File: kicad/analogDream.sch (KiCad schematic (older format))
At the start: 37 parts, among them P2 CONN_4X2, P4 CONN_7X2, P6 CONN_4X2, U1 AD8422, U2 TL074

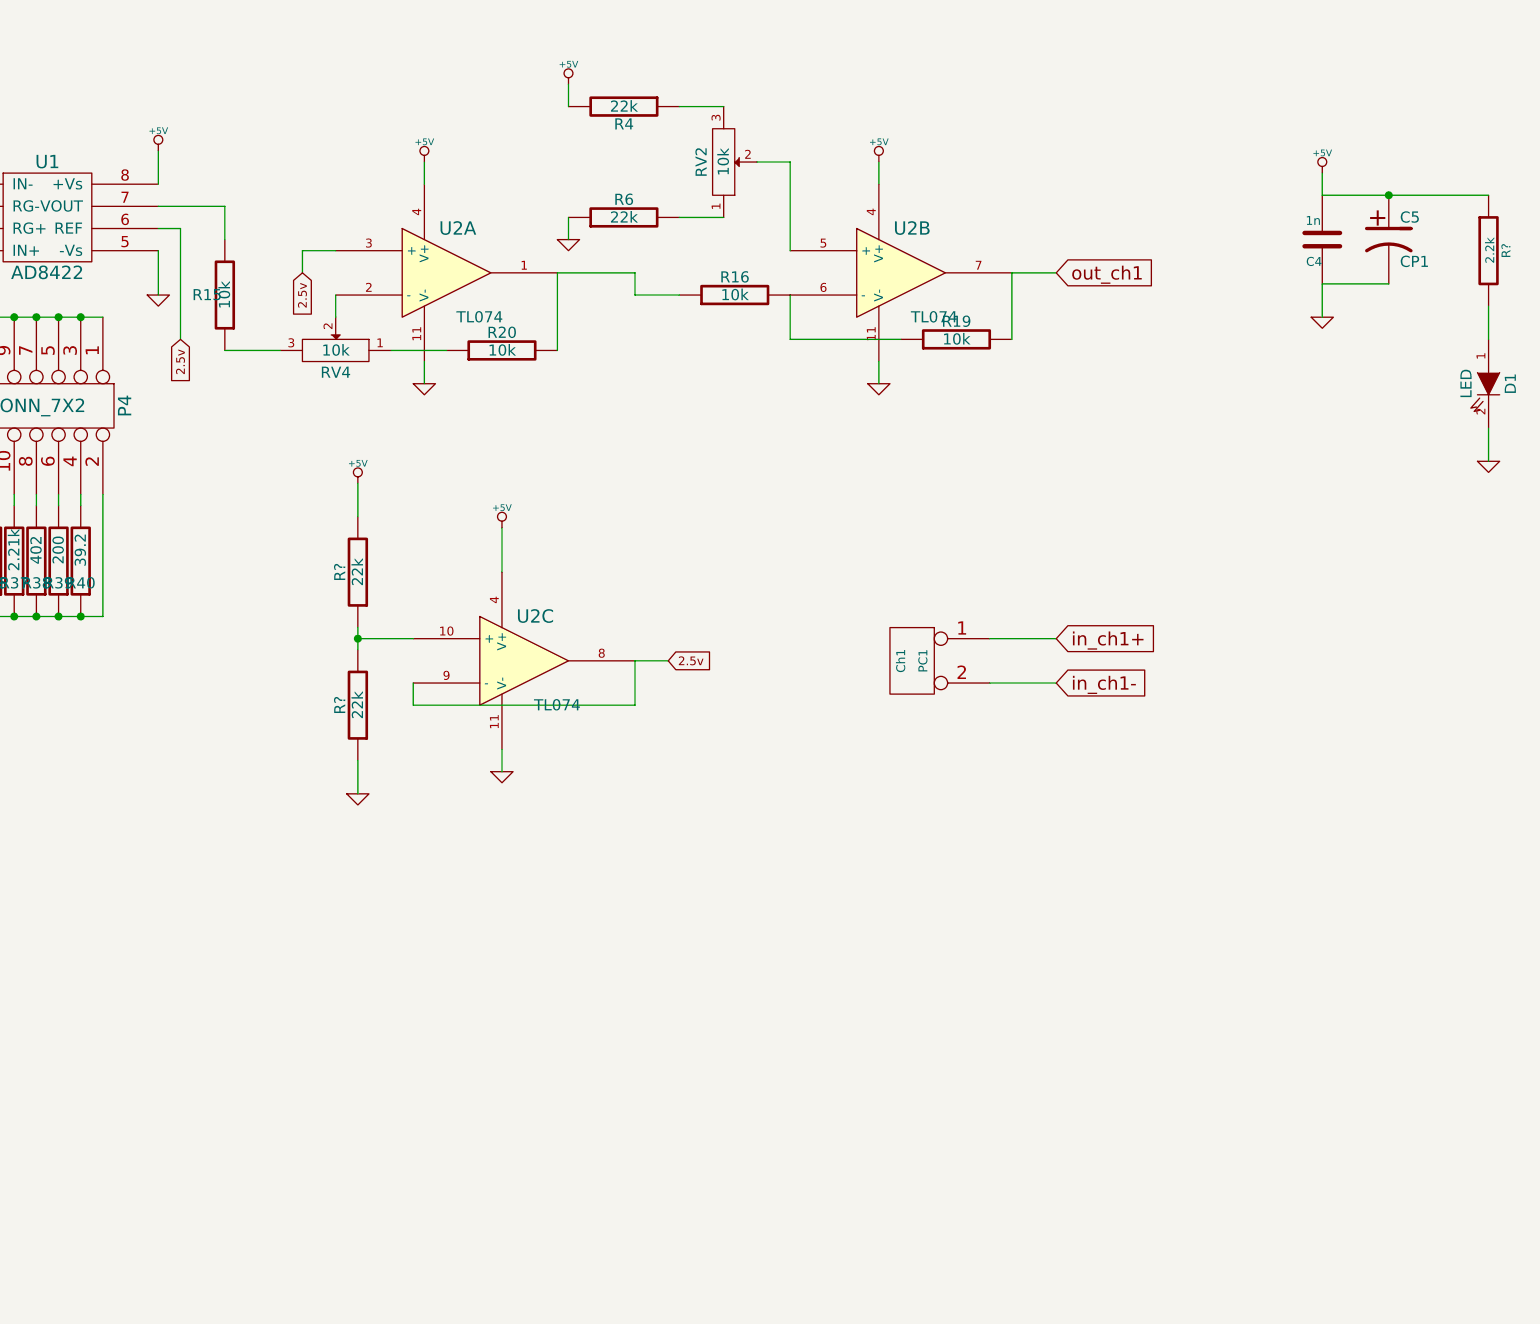
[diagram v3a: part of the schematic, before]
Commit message: Changed how offset voltage works
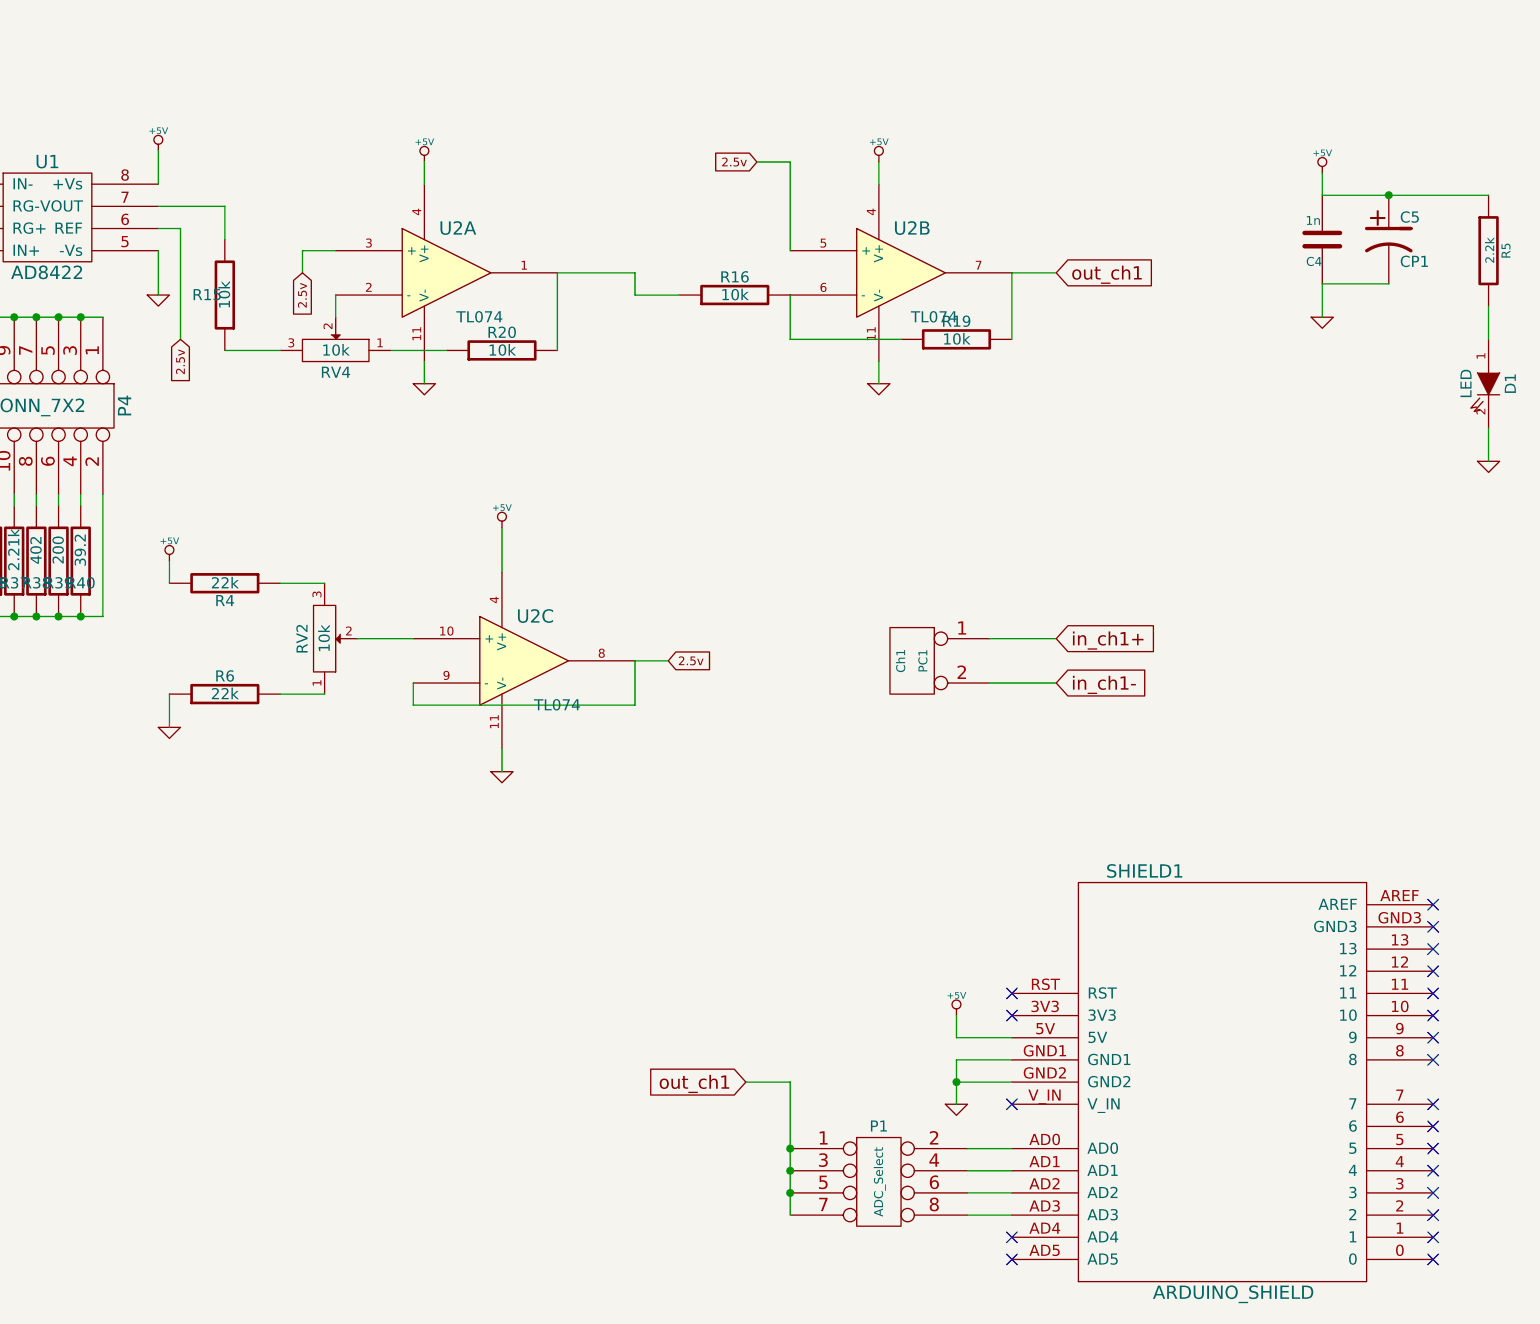
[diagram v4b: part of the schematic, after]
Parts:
- removed R? (x2): 22k, symbol R
- added P1: ADC_Select, symbol CONN_4X2
- added SHIELD1: ARDUINO_SHIELD, ~, symbol ARDUINO_SHIELD
- gave numbers to parts that had none: 1
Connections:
- net +5V: now also SHIELD1.5V
- net 2.5v: now also U2.5 (+)
- net GND: now also SHIELD1.GND1, SHIELD1.GND2
- net out_ch1: now also P1.1, P1.3, P1.5, P1.7
- net at RV2.2: now also U2.10 (+); no longer U2.5 (+)
- new net: P1.2, SHIELD1.AD0
- new net: P1.4, SHIELD1.AD1
- new net: P1.6, SHIELD1.AD2
- new net: P1.8, SHIELD1.AD3
- no-connect marks 0 -> 21
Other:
- moved on the sheet: R4, R6, RV2
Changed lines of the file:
@@
 	3450 1350 3450 1200
 Wire Wire Line
-	6000 1000 5800 1000
-Wire Wire Line
-	5800 1500 6000 1500
+	4200 3150 4000 3150
+Wire Wire Line
+	4000 3650 4200 3650
 Wire Wire Line
 	7300 2050 7300 1750
@@
 Wire Wire Line
 	6300 2050 6300 1850
-Wire Wire Line
-	5300 1500 5300 1600
 Wire Wire Line
 	6150 1250 6300 1250
@@
 L R R4
 U 1 1 4ECF00A1
-P 5550 1000
-F 0 "R4" V 5630 1000 50  0000 C CNN
-F 1 "22k" V 5550 1000 50  0000 C CNN
-F 2 "" H 5550 1000 60  0001 C CNN
-F 3 "" H 5550 1000 60  0001 C CNN
-	1    5550 1000
+P 3750 3150
+F 0 "R4" V 3830 3150 50  0000 C CNN
+F 1 "22k" V 3750 3150 50  0000 C CNN
+F 2 "" H 3750 3150 60  0001 C CNN
+F 3 "" H 3750 3150 60  0001 C CNN
+	1    3750 3150
 	0    1    1    0
 $EndComp
 $Comp
-L GND #PWR026
+L GND #PWR01
 U 1 1 4ECF0087
-P 5300 1600
-F 0 "#PWR026" H 5300 1600 30  0001 C CNN
-F 1 "GND" H 5300 1530 30  0001 C CNN
-F 2 "" H 5300 1600 60  0001 C CNN
-F 3 "" H 5300 1600 60  0001 C CNN
-	1    5300 1600
+P 3500 3800
+F 0 "#PWR01" H 3500 3800 30  0001 C CNN
+F 1 "GND" H 3500 3730 30  0001 C CNN
+F 2 "" H 3500 3800 60  0001 C CNN
+F 3 "" H 3500 3800 60  0001 C CNN
+	1    3500 3800
 	1    0    0    -1
 $EndComp
@@
 L R R6
 U 1 1 4ECF005D
-P 5550 1500
-F 0 "R6" V 5630 1500 50  0000 C CNN
-F 1 "22k" V 5550 1500 50  0000 C CNN
-F 2 "" H 5550 1500 60  0001 C CNN
-F 3 "" H 5550 1500 60  0001 C CNN
-	1    5550 1500
+P 3750 3650
+F 0 "R6" V 3830 3650 50  0000 C CNN
+F 1 "22k" V 3750 3650 50  0000 C CNN
+F 2 "" H 3750 3650 60  0001 C CNN
+F 3 "" H 3750 3650 60  0001 C CNN
+	1    3750 3650
 	0    -1   -1   0
 $EndComp
@@
 L POT RV2
 U 1 1 4ECF0010
-P 6000 1250
-F 0 "RV2" H 6000 1150 50  0000 C CNN
-F 1 "10k" H 6000 1250 50  0000 C CNN
-F 2 "" H 6000 1250 60  0001 C CNN
-F 3 "" H 6000 1250 60  0001 C CNN
-	1    6000 1250
+P 4200 3400
+F 0 "RV2" H 4200 3300 50  0000 C CNN
+F 1 "10k" H 4200 3400 50  0000 C CNN
+F 2 "" H 4200 3400 60  0001 C CNN
+F 3 "" H 4200 3400 60  0001 C CNN
+	1    4200 3400
 	0    1    -1   0
 $EndComp
@@
 $EndComp
 $Comp
-L R R?
-U 1 1 51EAD263
-P 4350 3100
-F 0 "R?" V 4430 3100 50  0000 C CNN
-F 1 "22k" V 4350 3100 50  0000 C CNN
-F 2 "" H 4350 3100 60  0001 C CNN
-F 3 "" H 4350 3100 60  0001 C CNN
-	1    4350 3100
-	-1   0    0    1
-$EndComp
-$Comp
-L R R?
-U 1 1 51EAD26C
-P 4350 3700
-F 0 "R?" V 4430 3700 50  0000 C CNN
-F 1 "22k" V 4350 3700 50  0000 C CNN
-F 2 "" H 4350 3700 60  0001 C CNN
-F 3 "" H 4350 3700 60  0001 C CNN
-	1    4350 3700
-	-1   0    0    1
-$EndComp
-Wire Wire Line
-	4350 3350 4350 3450
-$Comp
-L GND #PWR?
+L GND #PWR02
 U 1 1 51EAD2C8
 P 3450 1850
-F 0 "#PWR?" H 3450 1850 30  0001 C CNN
+F 0 "#PWR02" H 3450 1850 30  0001 C CNN
 F 1 "GND" H 3450 1780 30  0001 C CNN
 F 2 "" H 3450 1850 60  0001 C CNN
@@
 $EndComp
 $Comp
-L GND #PWR?
+L GND #PWR03
 U 1 1 51EAD321
 P 4650 2250
-F 0 "#PWR?" H 4650 2250 30  0001 C CNN
+F 0 "#PWR03" H 4650 2250 30  0001 C CNN
 F 1 "GND" H 4650 2180 30  0001 C CNN
 F 2 "" H 4650 2250 60  0001 C CNN
@@
 $EndComp
 $Comp
-L GND #PWR?
+L GND #PWR04
 U 1 1 51EAD327
 P 6700 2250
-F 0 "#PWR?" H 6700 2250 30  0001 C CNN
+F 0 "#PWR04" H 6700 2250 30  0001 C CNN
 F 1 "GND" H 6700 2180 30  0001 C CNN
 F 2 "" H 6700 2250 60  0001 C CNN
@@
 $EndComp
 $Comp
-L GND #PWR?
+L GND #PWR05
 U 1 1 51EAD32D
 P 5000 4000
-F 0 "#PWR?" H 5000 4000 30  0001 C CNN
+F 0 "#PWR05" H 5000 4000 30  0001 C CNN
 F 1 "GND" H 5000 3930 30  0001 C CNN
 F 2 "" H 5000 4000 60  0001 C CNN
@@
 $EndComp
 $Comp
-L +5V #PWR?
+L +5V #PWR06
 U 1 1 51EAD335
 P 3450 1200
-F 0 "#PWR?" H 3450 1290 20  0001 C CNN
+F 0 "#PWR06" H 3450 1290 20  0001 C CNN
 F 1 "+5V" H 3450 1290 30  0000 C CNN
 F 2 "" H 3450 1200 60  0000 C CNN
@@
 $EndComp
 $Comp
-L +5V #PWR?
+L +5V #PWR07
 U 1 1 51EAD342
 P 4650 1250
-F 0 "#PWR?" H 4650 1340 20  0001 C CNN
+F 0 "#PWR07" H 4650 1340 20  0001 C CNN
 F 1 "+5V" H 4650 1340 30  0000 C CNN
 F 2 "" H 4650 1250 60  0000 C CNN
@@
 $EndComp
 $Comp
-L +5V #PWR?
+L +5V #PWR08
 U 1 1 51EAD348
 P 6700 1250
-F 0 "#PWR?" H 6700 1340 20  0001 C CNN
+F 0 "#PWR08" H 6700 1340 20  0001 C CNN
 F 1 "+5V" H 6700 1340 30  0000 C CNN
 F 2 "" H 6700 1250 60  0000 C CNN
@@
 $EndComp
 $Comp
-L +5V #PWR?
+L +5V #PWR09
 U 1 1 51EAD34E
-P 5300 900
-F 0 "#PWR?" H 5300 990 20  0001 C CNN
-F 1 "+5V" H 5300 990 30  0000 C CNN
-F 2 "" H 5300 900 60  0000 C CNN
-F 3 "" H 5300 900 60  0000 C CNN
-	1    5300 900
-	1    0    0    -1
-$EndComp
-Wire Wire Line
-	5300 900  5300 1000
+P 3500 3050
+F 0 "#PWR09" H 3500 3140 20  0001 C CNN
+F 1 "+5V" H 3500 3140 30  0000 C CNN
+F 2 "" H 3500 3050 60  0000 C CNN
+F 3 "" H 3500 3050 60  0000 C CNN
+	1    3500 3050
+	1    0    0    -1
+$EndComp
+Wire Wire Line
+	3500 3050 3500 3150
 Wire Wire Line
 	4600 3400 4350 3400
-Connection ~ 4350 3400
 Wire Wire Line
 	4600 3600 4600 3700
@@
 	5000 3900 5000 4000
 $Comp
-L GND #PWR?
-U 1 1 51EAD4AC
-P 4350 4100
-F 0 "#PWR?" H 4350 4100 30  0001 C CNN
-F 1 "GND" H 4350 4030 30  0001 C CNN
-F 2 "" H 4350 4100 60  0001 C CNN
-F 3 "" H 4350 4100 60  0001 C CNN
-	1    4350 4100
-	1    0    0    -1
-$EndComp
-Wire Wire Line
-	4350 3950 4350 4100
-$Comp
-L +5V #PWR?
-U 1 1 51EAD50C
-P 4350 2700
-F 0 "#PWR?" H 4350 2790 20  0001 C CNN
-F 1 "+5V" H 4350 2790 30  0000 C CNN
-F 2 "" H 4350 2700 60  0000 C CNN
-F 3 "" H 4350 2700 60  0000 C CNN
-	1    4350 2700
-	1    0    0    -1
-$EndComp
-Wire Wire Line
-	4350 2700 4350 2850
-$Comp
-L +5V #PWR?
+L +5V #PWR012
 U 1 1 51EAD56D
 P 5000 2900
-F 0 "#PWR?" H 5000 2990 20  0001 C CNN
+F 0 "#PWR012" H 5000 2990 20  0001 C CNN
 F 1 "+5V" H 5000 2990 30  0000 C CNN
 F 2 "" H 5000 2900 60  0000 C CNN
@@
 $EndComp
 $Comp
-L +5V #PWR?
+L +5V #PWR013
 U 1 1 51FEDEB1
 P 8700 1300
-F 0 "#PWR?" H 8700 1390 20  0001 C CNN
+F 0 "#PWR013" H 8700 1390 20  0001 C CNN
 F 1 "+5V" H 8700 1390 30  0000 C CNN
 F 2 "" H 8700 1300 60  0000 C CNN
@@
 $EndComp
 $Comp
-L GND #PWR?
+L GND #PWR014
 U 1 1 51FEDEB7
 P 8700 1950
-F 0 "#PWR?" H 8700 1950 30  0001 C CNN
+F 0 "#PWR014" H 8700 1950 30  0001 C CNN
 F 1 "GND" H 8700 1880 30  0001 C CNN
 F 2 "" H 8700 1950 60  0001 C CNN
@@
 	8700 1800 9000 1800
 $Comp
-L R R?
+L R R5
 U 1 1 51FEE0BE
 P 9450 1650
-F 0 "R?" V 9530 1650 40  0000 C CNN
+F 0 "R5" V 9530 1650 40  0000 C CNN
 F 1 "2.2k" V 9457 1651 40  0000 C CNN
 F 2 "~" V 9380 1650 30  0000 C CNN
@@
 	9450 1900 9450 2050
 $Comp
-L GND #PWR?
+L GND #PWR015
 U 1 1 51FEE1AC
 P 9450 2600
-F 0 "#PWR?" H 9450 2600 30  0001 C CNN
+F 0 "#PWR015" H 9450 2600 30  0001 C CNN
 F 1 "GND" H 9450 2530 30  0001 C CNN
 F 2 "" H 9450 2600 60  0001 C CNN
@@
 Wire Wire Line
 	7500 3400 7200 3400
+$Comp
+L ARDUINO_SHIELD SHIELD1
+U 1 1 51FEE48A
+P 8250 5400
+F 0 "SHIELD1" H 7900 6350 60  0000 C CNN
+F 1 "ARDUINO_SHIELD" H 8300 4450 60  0000 C CNN
+F 2 "~" H 8250 5400 60  0000 C CNN
+F 3 "~" H 8250 5400 60  0000 C CNN
+	1    8250 5400
+	1    0    0    -1
+$EndComp
+$Comp
+L CONN_4X2 P1
+U 1 1 51FEE499
+P 6700 5850
+F 0 "P1" H 6700 6100 50  0000 C CNN
+F 1 "ADC_Select" V 6700 5850 40  0000 C CNN
+F 2 "" H 6700 5850 60  0000 C CNN
+F 3 "" H 6700 5850 60  0000 C CNN
+	1    6700 5850
+	1    0    0    -1
+$EndComp
+Wire Wire Line
+	7100 5700 7300 5700
+Wire Wire Line
+	7100 5800 7300 5800
+Wire Wire Line
+	7100 5900 7300 5900
+Wire Wire Line
+	7100 6000 7300 6000
+Text GLabel 6100 5400 0    60   Input ~ 0
+out_ch1
+Wire Wire Line
+	6100 5400 6300 5400
+Wire Wire Line
+	6300 5400 6300 6000
+Connection ~ 6300 5700
+Connection ~ 6300 5800
+Connection ~ 6300 5900
+$Comp
+L +5V #PWR016
+U 1 1 51FEE8F9
+P 7050 5100
+F 0 "#PWR016" H 7050 5190 20  0001 C CNN
+F 1 "+5V" H 7050 5190 30  0000 C CNN
+F 2 "" H 7050 5100 60  0000 C CNN
+F 3 "" H 7050 5100 60  0000 C CNN
+	1    7050 5100
+	1    0    0    -1
+$EndComp
+Wire Wire Line
+	7300 5200 7050 5200
+Wire Wire Line
+	7050 5200 7050 5100
+Wire Wire Line
+	7300 5300 7050 5300
+Wire Wire Line
+	7050 5300 7050 5500
+Wire Wire Line
+	7300 5400 7050 5400
+Connection ~ 7050 5400
+NoConn ~ 9200 4600
+NoConn ~ 9200 4700
+NoConn ~ 9200 4800
+NoConn ~ 9200 4900
+NoConn ~ 9200 5000
+NoConn ~ 9200 5100
+NoConn ~ 9200 5200
+NoConn ~ 9200 5300
+NoConn ~ 9200 5500
+NoConn ~ 9200 5600
+NoConn ~ 9200 5700
+NoConn ~ 9200 5800
+NoConn ~ 9200 5900
+NoConn ~ 9200 6000
+NoConn ~ 9200 6100
+NoConn ~ 9200 6200
+NoConn ~ 7300 6100
+NoConn ~ 7300 6200
+NoConn ~ 7300 5500
+NoConn ~ 7300 5100
+NoConn ~ 7300 5000
+$Comp
+L GND #PWR017
+U 1 1 51FEEC4E
+P 7050 5500
+F 0 "#PWR017" H 7050 5500 30  0001 C CNN
+F 1 "GND" H 7050 5430 30  0001 C CNN
+F 2 "" H 7050 5500 60  0001 C CNN
+F 3 "" H 7050 5500 60  0001 C CNN
+	1    7050 5500
+	1    0    0    -1
+$EndComp
+Wire Wire Line
+	3500 3650 3500 3800
+Text GLabel 6150 1250 0    39   Input ~ 0
+2.5v
 $EndSCHEMATC

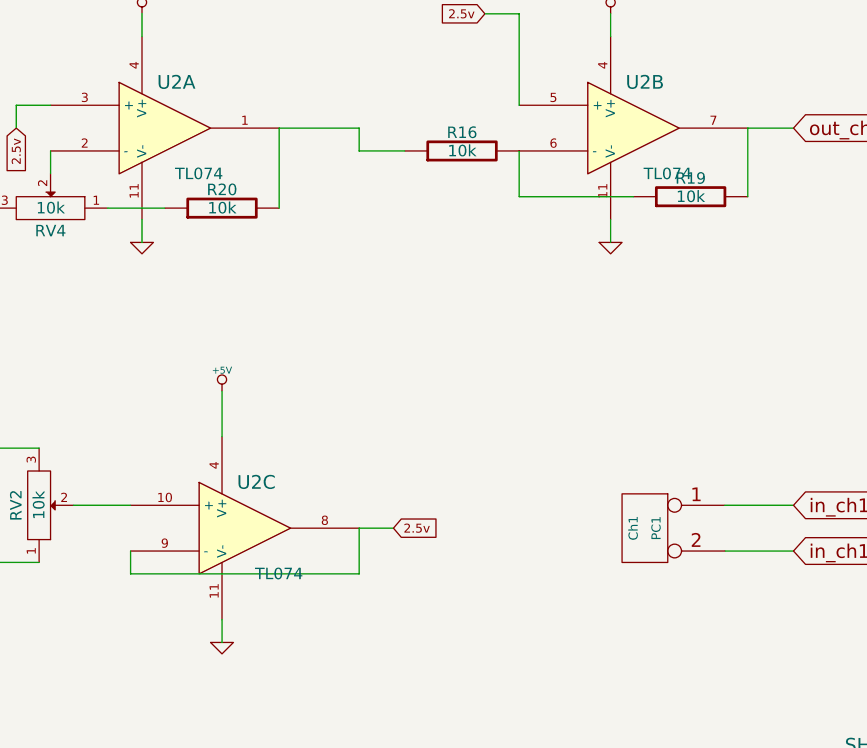
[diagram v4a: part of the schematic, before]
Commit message: Did some board layout, changed quad opamp
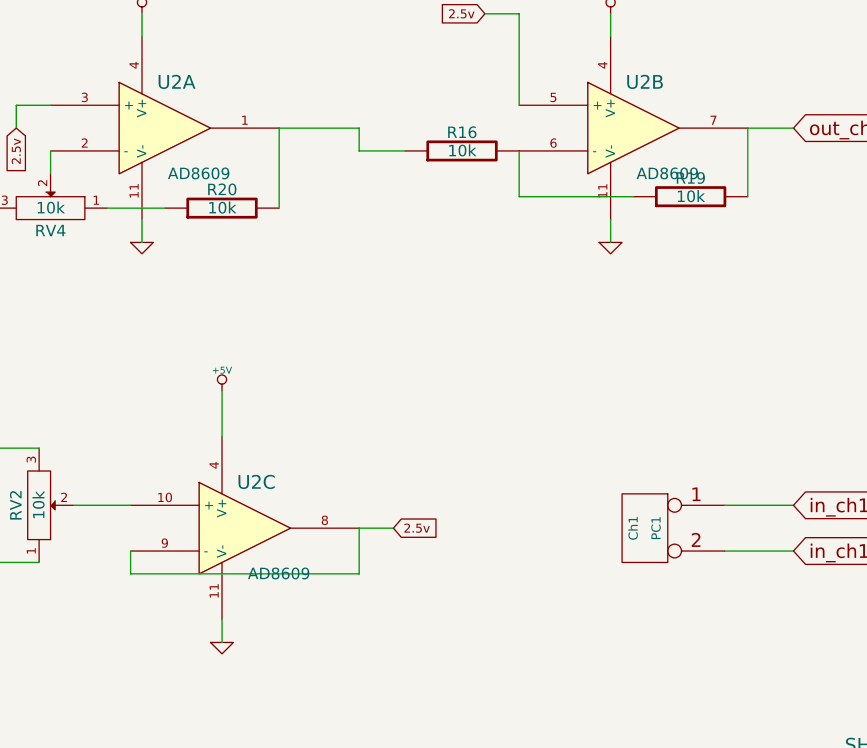
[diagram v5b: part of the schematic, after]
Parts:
- U2: value TL074 -> AD8609
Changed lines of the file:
@@
 Sheet 1 1
 Title "Analog Dream Board Shield"
-Date "4 aug 2013"
+Date "5 aug 2013"
 Rev ""
 Comp "Visgence Technologies"
@@
 	5000 3900 5000 4000
 $Comp
-L +5V #PWR012
+L +5V #PWR010
 U 1 1 51EAD56D
 P 5000 2900
-F 0 "#PWR012" H 5000 2990 20  0001 C CNN
+F 0 "#PWR010" H 5000 2990 20  0001 C CNN
 F 1 "+5V" H 5000 2990 30  0000 C CNN
 F 2 "" H 5000 2900 60  0000 C CNN
@@
 P 5100 3500
 F 0 "U2" H 5150 3700 60  0000 C CNN
-F 1 "TL074" H 5250 3300 50  0000 C CNN
+F 1 "AD8609" H 5250 3300 50  0000 C CNN
 F 2 "" H 5100 3500 60  0000 C CNN
 F 3 "" H 5100 3500 60  0000 C CNN
@@
 P 4750 1750
 F 0 "U2" H 4800 1950 60  0000 C CNN
-F 1 "TL074" H 4900 1550 50  0000 C CNN
+F 1 "AD8609" H 4900 1550 50  0000 C CNN
 F 2 "" H 4750 1750 60  0000 C CNN
 F 3 "" H 4750 1750 60  0000 C CNN
@@
 P 6800 1750
 F 0 "U2" H 6850 1950 60  0000 C CNN
-F 1 "TL074" H 6950 1550 50  0000 C CNN
+F 1 "AD8609" H 6950 1550 50  0000 C CNN
 F 2 "" H 6800 1750 60  0000 C CNN
 F 3 "" H 6800 1750 60  0000 C CNN
@@
 $EndComp
 $Comp
-L +5V #PWR013
+L +5V #PWR011
 U 1 1 51FEDEB1
 P 8700 1300
-F 0 "#PWR013" H 8700 1390 20  0001 C CNN
+F 0 "#PWR011" H 8700 1390 20  0001 C CNN
 F 1 "+5V" H 8700 1390 30  0000 C CNN
 F 2 "" H 8700 1300 60  0000 C CNN
@@
 $EndComp
 $Comp
-L GND #PWR014
+L GND #PWR012
 U 1 1 51FEDEB7
 P 8700 1950
-F 0 "#PWR014" H 8700 1950 30  0001 C CNN
+F 0 "#PWR012" H 8700 1950 30  0001 C CNN
 F 1 "GND" H 8700 1880 30  0001 C CNN
 F 2 "" H 8700 1950 60  0001 C CNN
@@
 	9450 1900 9450 2050
 $Comp
-L GND #PWR015
+L GND #PWR013
 U 1 1 51FEE1AC
 P 9450 2600
-F 0 "#PWR015" H 9450 2600 30  0001 C CNN
+F 0 "#PWR013" H 9450 2600 30  0001 C CNN
 F 1 "GND" H 9450 2530 30  0001 C CNN
 F 2 "" H 9450 2600 60  0001 C CNN
@@
 Connection ~ 6300 5900
 $Comp
-L +5V #PWR016
+L +5V #PWR014
 U 1 1 51FEE8F9
 P 7050 5100
-F 0 "#PWR016" H 7050 5190 20  0001 C CNN
+F 0 "#PWR014" H 7050 5190 20  0001 C CNN
 F 1 "+5V" H 7050 5190 30  0000 C CNN
 F 2 "" H 7050 5100 60  0000 C CNN
@@
 NoConn ~ 7300 5000
 $Comp
-L GND #PWR017
+L GND #PWR015
 U 1 1 51FEEC4E
 P 7050 5500
-F 0 "#PWR017" H 7050 5500 30  0001 C CNN
+F 0 "#PWR015" H 7050 5500 30  0001 C CNN
 F 1 "GND" H 7050 5430 30  0001 C CNN
 F 2 "" H 7050 5500 60  0001 C CNN
